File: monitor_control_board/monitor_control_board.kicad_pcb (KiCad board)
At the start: 2 copper layers, 50 x 65 mm, 12 parts, among them J1 Conn_01x08_Male, J2 Conn_01x08_Male, J3 Conn_01x08_Male, SW1 SW_Push, SW2 SW_Push, SW3 SW_Push, SW4 SW_Push, SW5 SW_Push, SW6 SW_Push

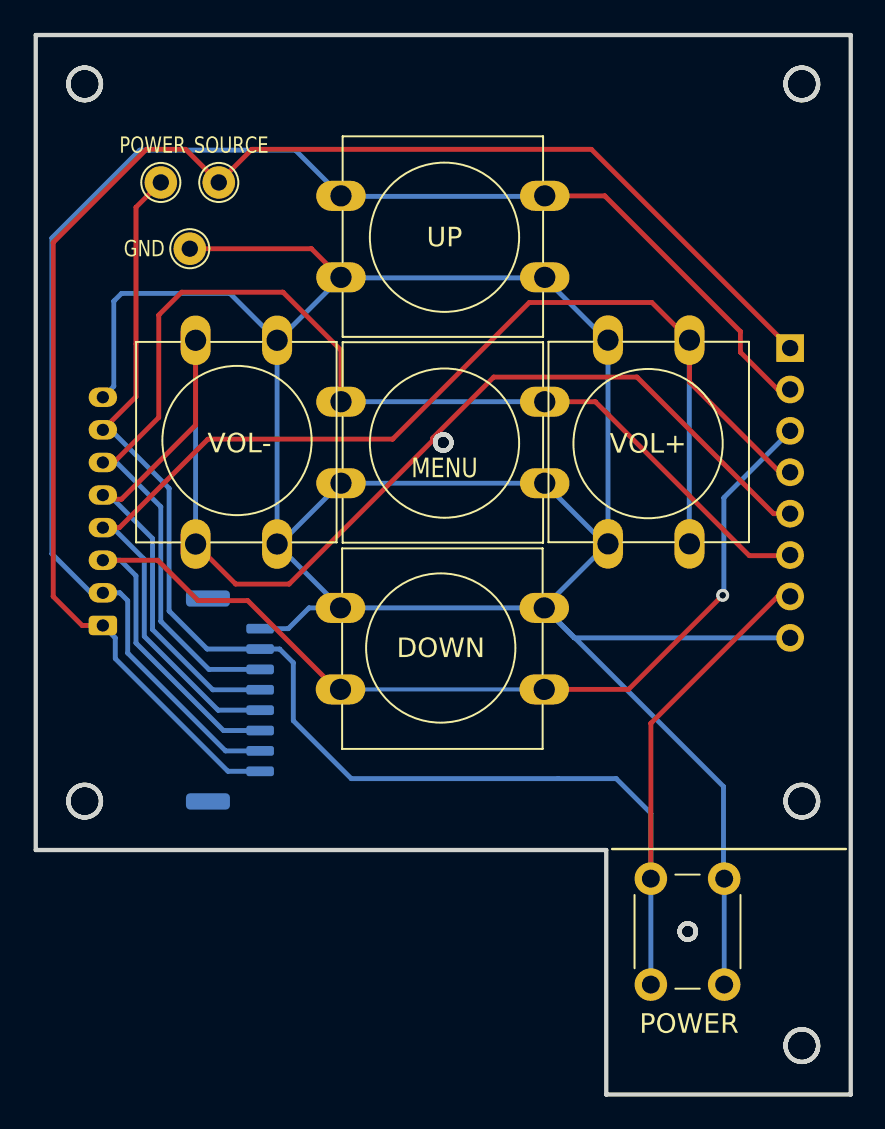
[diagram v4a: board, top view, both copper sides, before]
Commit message: OSD 컨트롤 보드에 IR수신 파트 추가
Signed-off-by: Ju, Gyeong-min <jcmh74@gmail.com>
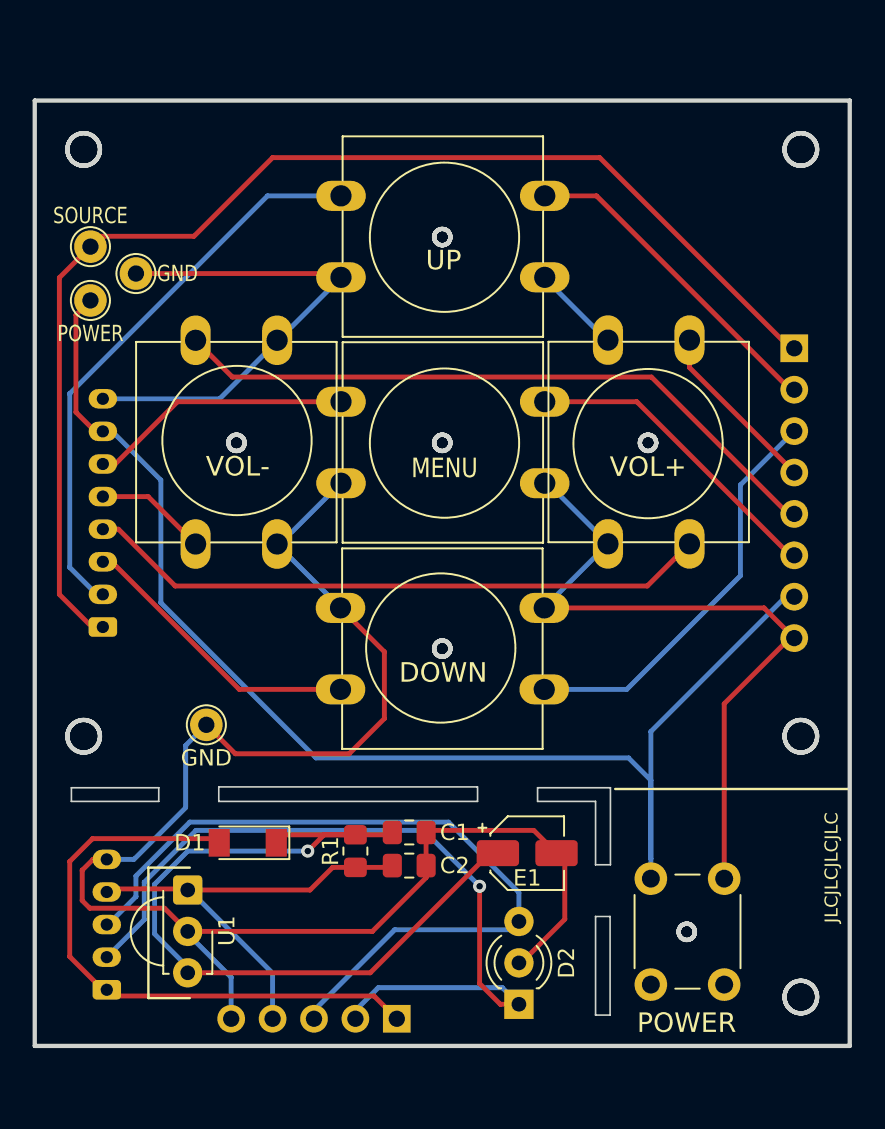
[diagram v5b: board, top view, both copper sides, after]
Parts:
- removed J1: Conn_01x08_Male, Connector_JST:JST_GH_SM08B-GHS-TB_1x08-1MP_P1.25mm_Horizontal
- added C1: 0.1uF-0805-Y5V-50V, Capacitor_SMD:C_0805_2012Metric_Pad1.18x1.45mm_HandSolder, F.Cu at (151.6, 106.7)
- added C2: 560pF-0805-X7R-16V, Capacitor_SMD:C_0805_2012Metric_Pad1.18x1.45mm_HandSolder, F.Cu at (151.6, 108.7)
- added D1: LL4148, Diode_SMD:D_MiniMELF, F.Cu at (141.7, 107.3)
- added D2: LED_Dual_AKA, LED_THT:LED_D3.0mm-3, F.Cu at (158.4, 117.2)
- added E1: 47uF-16V, Capacitor_SMD:CP_Elec_4x5.4, F.Cu at (158.9, 108.0)
- added J5: Conn_01x05_Male, Connector_PinHeader_2.54mm:PinHeader_1x05_P2.54mm_Vertical, B.Cu at (150.9, 118.1)
- added J6: Conn_01x05_Male, Connector_JST:JST_PH_S5B-PH-K_1x05_P2.00mm_Horizontal, B.Cu at (133.1, 116.3)
- added R1: 5K1-0805, Resistor_SMD:R_0805_2012Metric_Pad1.20x1.40mm_HandSolder, F.Cu at (148.3, 107.8)
- added TP4: TestPoint, TestPoint:TestPoint_THTPad_D2.0mm_Drill1.0mm, F.Cu at (139.2, 100.1)
- added U1: TSSP58038, OptoDevice:Vishay_MINICAST-3Pin, F.Cu at (138.0, 110.2)
- moved TP1 8.80 mm to (132.1, 70.7)
- moved TP3 8.43 mm to (132.1, 74.0)
- moved TP2 3.64 mm to (134.9, 72.4)
- moved J2 0.25 mm to (175.3, 77.0)
- moved J3 0.09 mm to (132.8, 94.1)
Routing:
- net /LED_R: track 0.00 -> 49.3 mm, vias 0 -> 1
- net Net-(C1-Pad1): track 0.00 -> 49.3 mm, vias 0 -> 1
- net /LED_G: track 0.00 -> 47.5 mm
- net /MENU: track 77.8 -> 35.4 mm
- net /VOL_M: track 88.7 -> 48.0 mm
- net /UP: track 93.4 -> 55.2 mm
- net +5V: track 0.00 -> 37.3 mm
- net /VOL_P: track 83.2 -> 49.3 mm
- net /DOWN: track 71.9 -> 43.0 mm, vias 1 -> 0
- net /IRIN: track 0.00 -> 28.4 mm
- net /SOURCE: track 93.9 -> 75.6 mm
- net /POWER: track 98.3 -> 82.3 mm
- net GND: track 171.9 -> 175.3 mm
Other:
- board size 50 x 65 mm -> 50 x 58 mm
- board text added: "5V"
- board text added: "IR"
- board text added: "IR Receiver Part"
- board text added: "LG"
- board text added: "LR"
- board text added: "Monitor OSD Control Board"
- board text added: "Rev.4"
- board text removed: "Monitor Control Board Rev.3"

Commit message: PCB 배선 최적화
Signed-off-by: Ju, Gyeong-min <jcmh74@gmail.com>
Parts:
- moved E1 2.55 mm to (156.3, 108.2)
- moved R1 1.80 mm to (146.6, 107.6)
- moved C1 1.42 mm to (150.2, 106.4)
- moved C2 1.40 mm to (150.2, 108.7)
- moved J5 1.27 mm to (152.1, 118.1)
- moved TP4 1.02 mm to (138.2, 100.1)
- moved U1 0.15 mm to (138.0, 110.4)
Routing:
- net Net-(C1-Pad1): track 49.3 -> 34.0 mm, vias 1 -> 0
- net /LED_G: track 47.5 -> 33.0 mm, vias 0 -> 1
- net /LED_R: track 49.3 -> 38.0 mm, vias 1 -> 0
- net GND: track 175.3 -> 179.5 mm, vias 0 -> 1
- net +5V: track 37.3 -> 41.1 mm
- net /IRIN: track 28.4 -> 27.7 mm
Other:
- outline, holes or cut-outs redrawn
- board text added: "47uF"
- board text added: "C1 - 0.1uF C2 - 560pF R1 - 5.1k"
- board text added: "PWR"
- board text added: "SR"
- board text added: "▲ If not used, SHORT it."
- board text removed: "SOURCE"

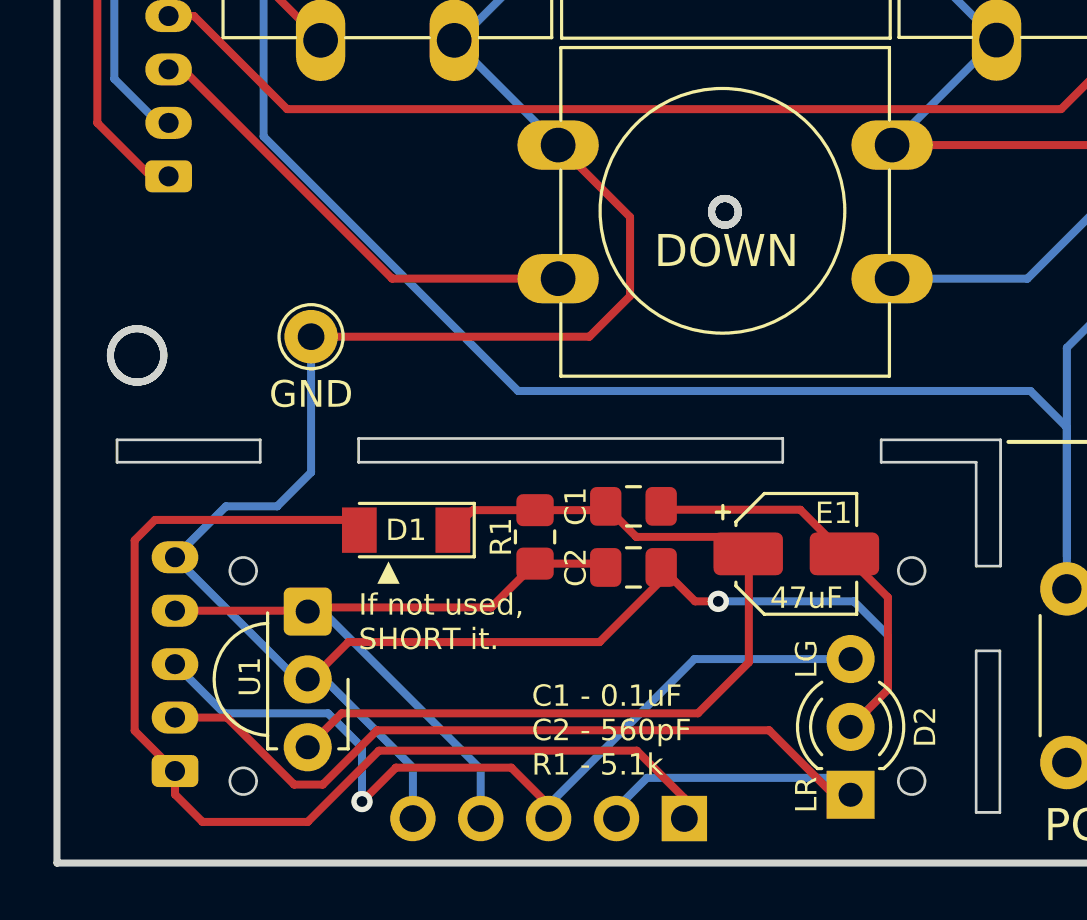
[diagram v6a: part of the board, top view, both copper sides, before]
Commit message: 모니터 osd 컨트롤 보드 배선 최적화
Signed-off-by: Ju, Gyeong-min <jcmh74@gmail.com>
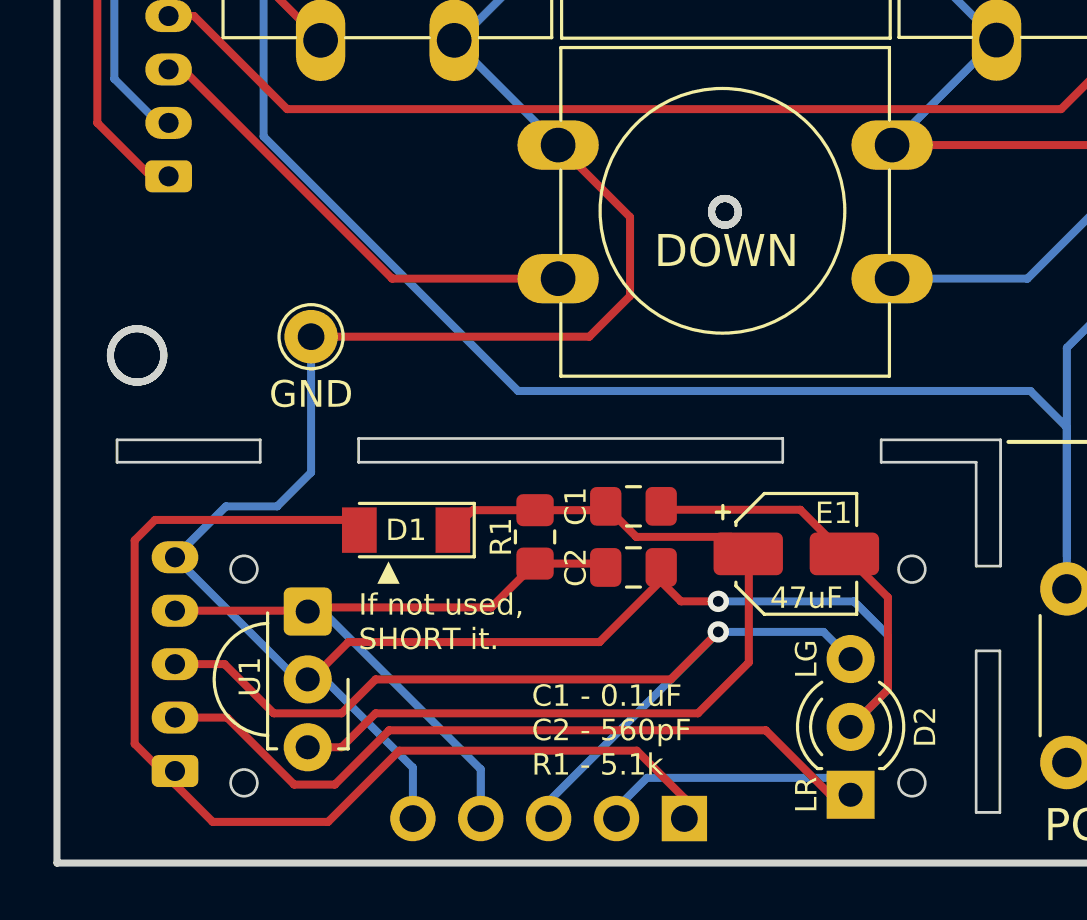
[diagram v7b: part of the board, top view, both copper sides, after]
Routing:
- net /LED_G: track 33.0 -> 37.3 mm
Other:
- outline, holes or cut-outs redrawn

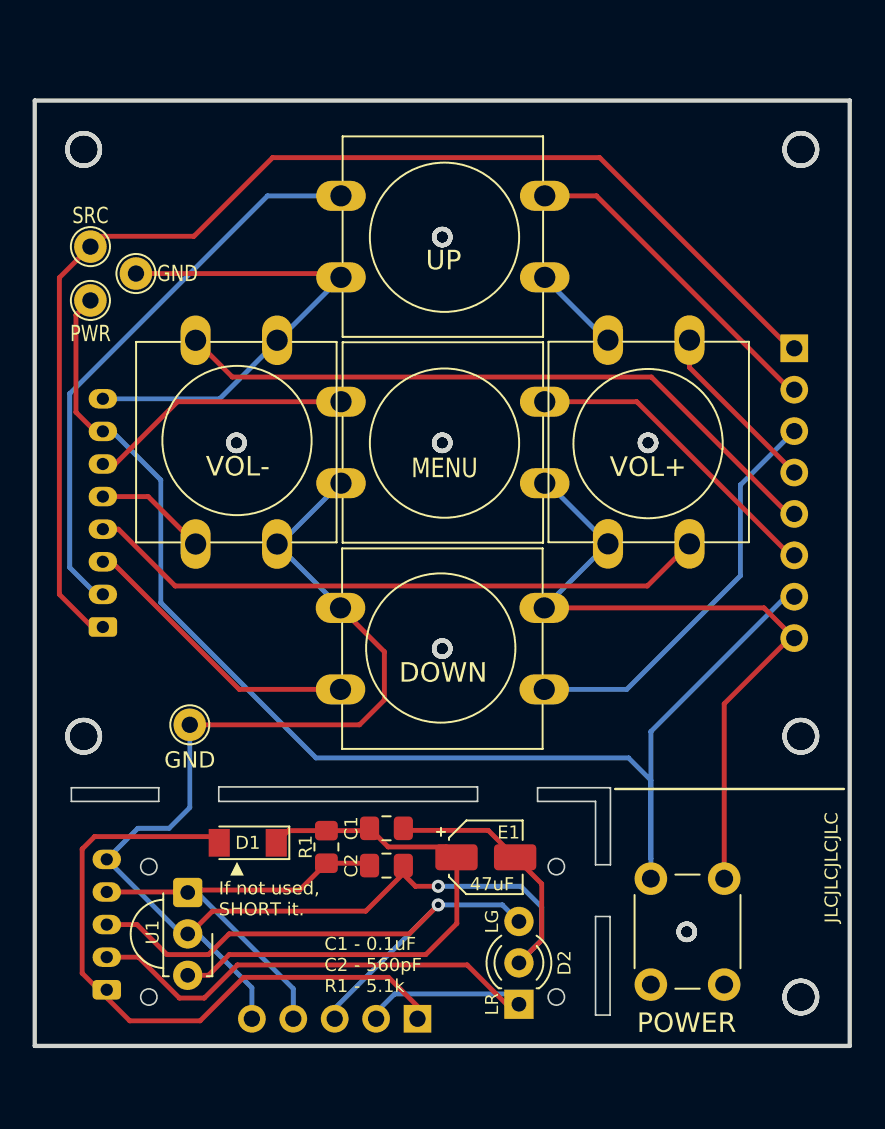
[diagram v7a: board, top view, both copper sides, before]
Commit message: osd 컨트롤 보드 좌표 미세 보정
Signed-off-by: Ju, Gyeong-min <jcmh74@gmail.com>
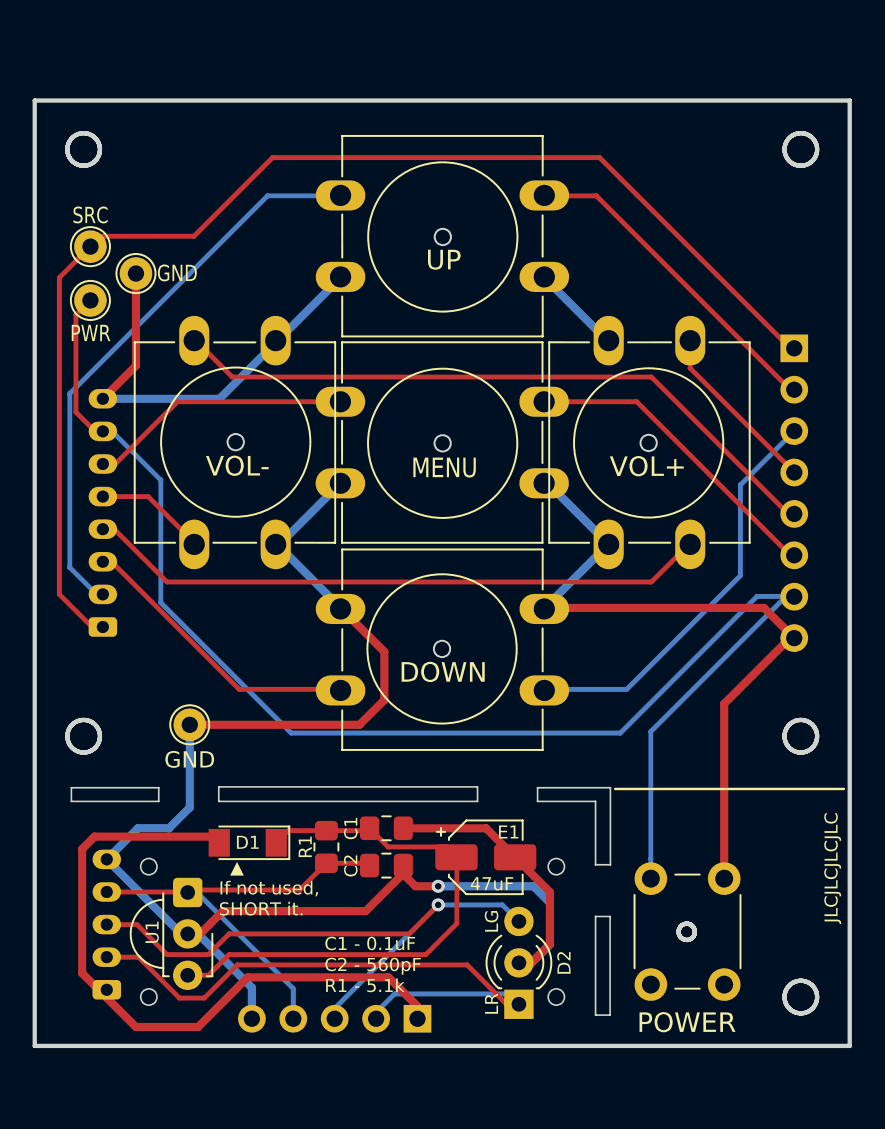
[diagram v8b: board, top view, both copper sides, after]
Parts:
- SW1, SW2, SW3, SW4, SW5: footprint Button_Switch_THT:SW_PUSH-12mm -> monitor_control_board_library:SW_PUSH-12mm_Complex
- moved SW1 0.09 mm to (138.4, 89.0)
- moved SW4 0.06 mm to (159.9, 98.0)
- moved SW5 0.06 mm to (168.9, 76.5)
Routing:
- net /POWER: track 82.3 -> 88.5 mm
- net GND: track 179.8 -> 178.4 mm
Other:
- outline, holes or cut-outs redrawn
